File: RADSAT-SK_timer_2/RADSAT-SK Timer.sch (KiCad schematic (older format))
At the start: 70 parts, among them J101 Conn_02x26_Odd_Even, J103 Conn_02x26_Odd_Even, Q101 IRLML2060, Q102 IRLML2060, Q103 IRLML2060, Q104 IRLML2060, Q105 IRLML2060, Q106 IRLML2060, Q107 IRLML2060, Q108 IRLML2060, Q109 IRLML2060, U101 LM397MF, U102 LM397MF, U103 LM397MF, U104 CD4052B

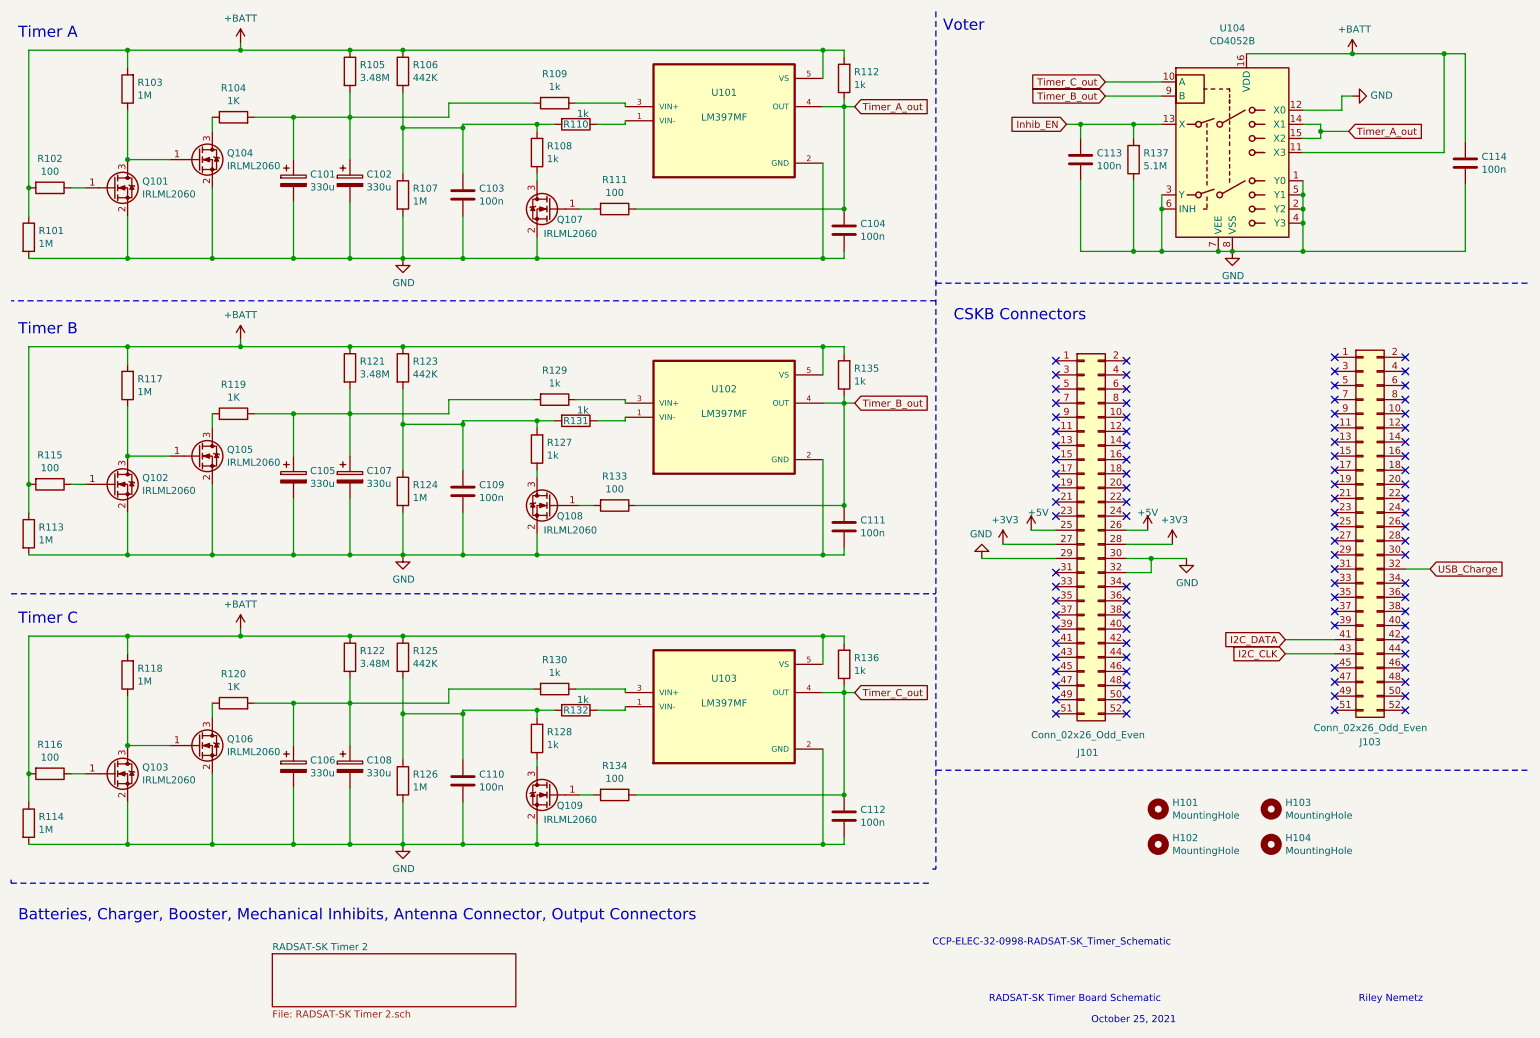
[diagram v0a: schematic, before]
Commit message: changed RBF logic and added footprint for J202
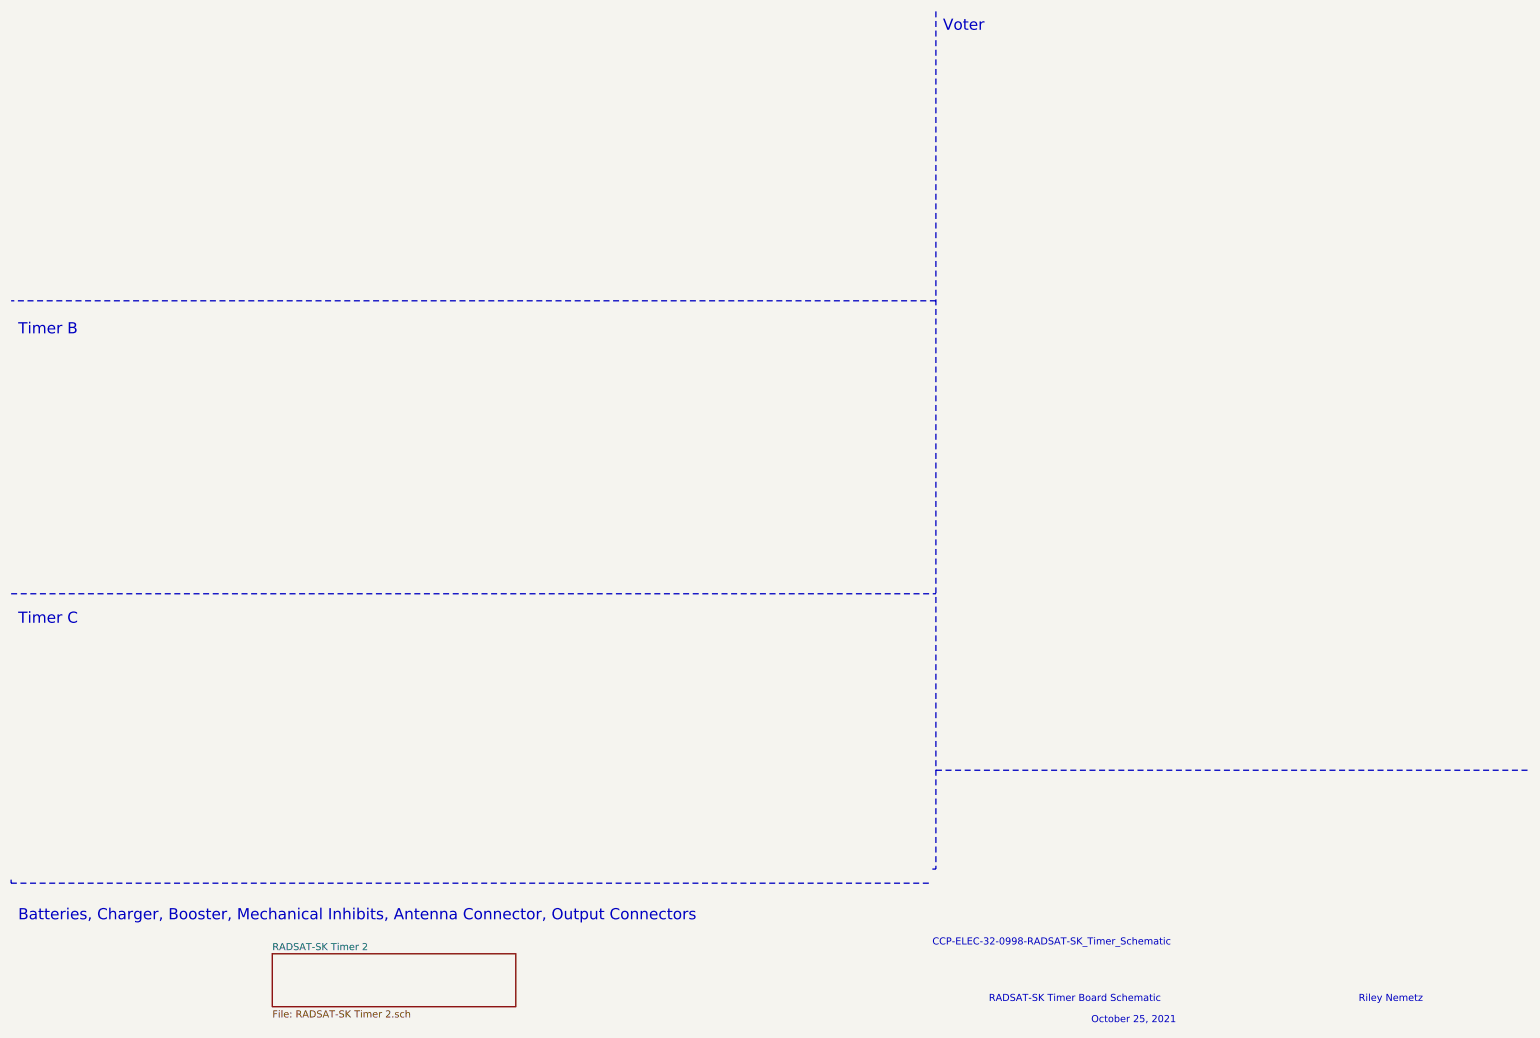
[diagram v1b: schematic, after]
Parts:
- removed C101, C102, C105, C106, C107, C108: 330u, Capacitor_Tantalum_SMD:CP_EIA-7343-30_AVX-N_Pad2.25x2.55mm_HandSolder, symbol Device:CP
- removed C103, C104, C109, C110, C111, C112, C113, C114: 100n, Capacitor_SMD:C_0805_2012Metric, symbol Device:C
- removed H101, H102, H103, H104: MountingHole, MountingHole:MountingHole_3.2mm_M3_ISO7380_Pad_TopBottom, symbol Mechanical:MountingHole
- removed J101, J103: Conn_02x26_Odd_Even, Connector_PinSocket_2.54mm:PinSocket_2x26_P2.54mm_Vertical, symbol Connector_Generic:Conn_02x26_Odd_Even
- removed Q101, Q102, Q103, Q104, Q105, Q106, Q107, Q108, Q109: IRLML2060, Package_TO_SOT_SMD:SOT-23_Handsoldering, symbol Transistor_FET:IRLML2060
- removed R101, R103, R107, R113, R114, R117, R118, R124, R126: 1M, Resistor_SMD:R_0805_2012Metric, symbol Device:R
- removed R102, R111, R115, R116, R133, R134: 100, Resistor_SMD:R_0805_2012Metric, symbol Device:R
- removed R104, R119, R120: 1K, Resistor_SMD:R_0805_2012Metric, symbol Device:R
- removed R105, R121, R122: 3.48M, Resistor_SMD:R_0805_2012Metric, symbol Device:R
- removed R106, R123, R125: 442K, Resistor_SMD:R_0805_2012Metric, symbol Device:R
- removed R108, R109, R110, R112, R127, R128, R129, R130, R131, R132, R135, R136: 1k, Resistor_SMD:R_0805_2012Metric, symbol Device:R
- removed R137: 5.1M, Resistor_SMD:R_0805_2012Metric, symbol Device:R
- removed U101, U102, U103: LM397MF, Package_TO_SOT_SMD:TSOT-23-5_HandSoldering, symbol LM397MF:LM397MF
- removed U104: CD4052B, Package_SO:TSSOP-16_4.4x5mm_P0.65mm, symbol Analog_Switch:CD4052B
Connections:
- no-connect marks 94 -> 0
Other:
- note removed: "CSKB Connectors"
- note removed: "Timer A"
